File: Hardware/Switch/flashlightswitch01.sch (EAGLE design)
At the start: 11 parts

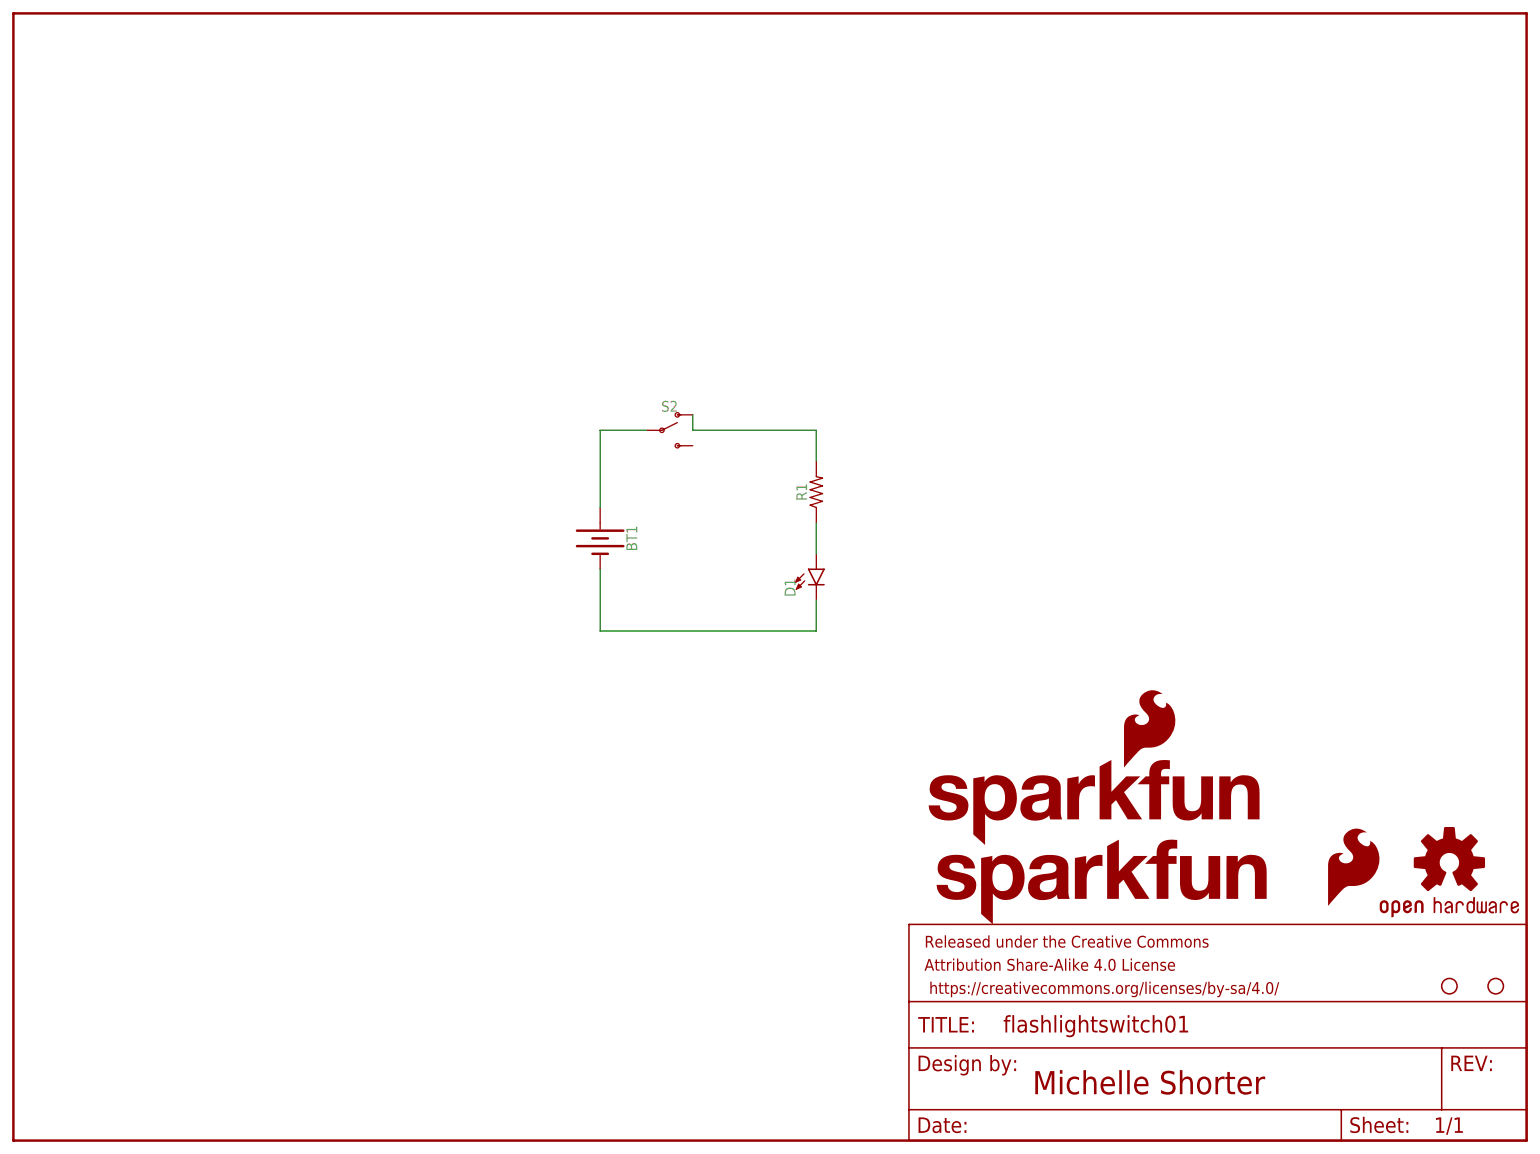
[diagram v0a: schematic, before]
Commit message: Post Proto Review
Added Buzzard labels, changed to different coin cell battery holder, moved schematic to back of board and other changes.
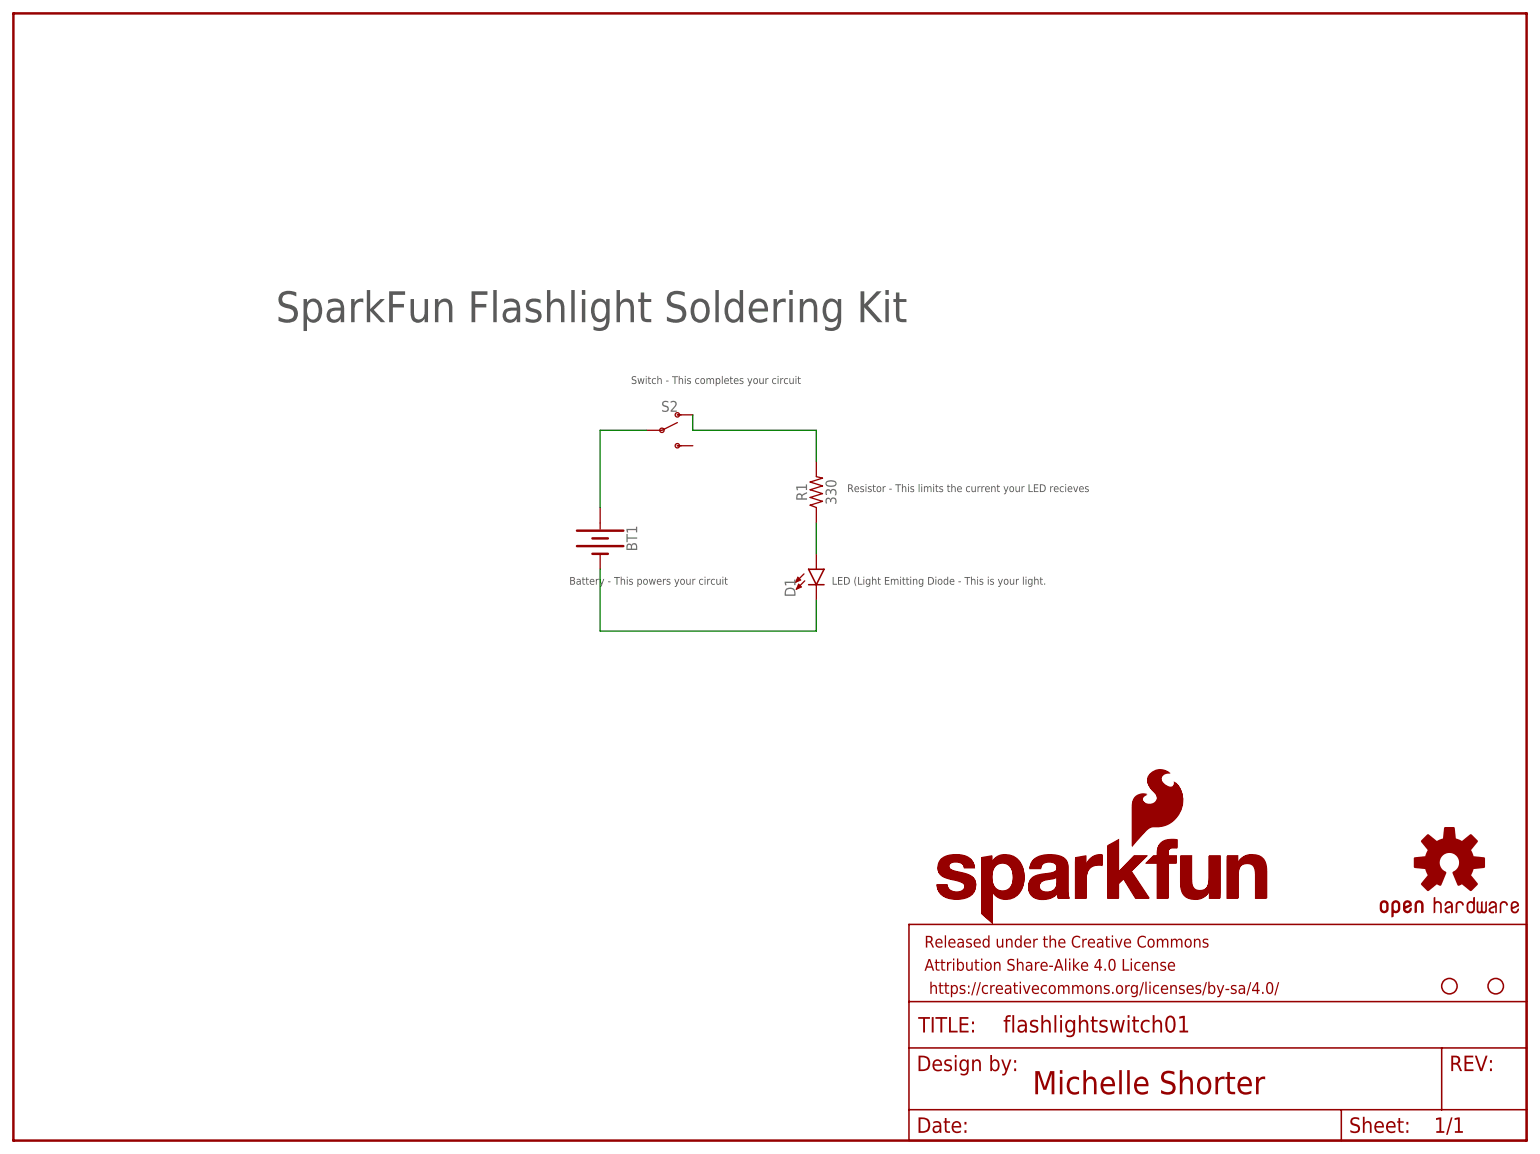
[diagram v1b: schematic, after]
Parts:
- R1: value (none) -> 330
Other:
- note added: "Battery - This powers your circuit"
- note added: "LED (Light Emitting Diode - This is your light."
- note added: "Resistor - This limits the current your LED recieves"
- note added: "SparkFun Flashlight Soldering Kit"
- note added: "Switch - This completes your circuit"
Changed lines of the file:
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@@
 <part name="LOGO1" library="SparkFun-Aesthetics" deviceset="OSHW-LOGO" device="S"/>
 <part name="D1" library="SparkFun-LED" deviceset="LED" device="5MM-KIT"/>
-<part name="R1" library="SparkFun-Resistors" deviceset="RESISTOR" device="AXIAL-0.3-KIT" value=" "/>
+<part name="R1" library="SparkFun-Resistors" deviceset="RESISTOR" device="AXIAL-0.3-KIT" value="330"/>
 <part name="LOGO2" library="SparkFun-Aesthetics" deviceset="SFE_LOGO_FLAME" device=".1_INCH"/>
 <part name="H1" library="SparkFun-Hardware" deviceset="STAND-OFF" device=""/>
@@
 <plain>
 <text x="167.64" y="7.62" size="3.81" layer="94">Michelle Shorter</text>
+<text x="43.18" y="134.62" size="5.08" layer="97" font="vector">SparkFun Flashlight Soldering Kit</text>
+<text x="134.62" y="91.44" size="1.27" layer="97">LED (Light Emitting Diode - This is your light.</text>
+<text x="137.16" y="106.68" size="1.27" layer="97">Resistor - This limits the current your LED recieves</text>
+<text x="101.6" y="124.46" size="1.27" layer="97">Switch - This completes your circuit</text>
+<text x="91.44" y="91.44" size="1.27" layer="97">Battery - This powers your circuit</text>
 </plain>
 <instances>
@@
 <instance part="D1" gate="G$1" x="132.08" y="93.98"/>
 <instance part="R1" gate="G$1" x="132.08" y="106.68" rot="R90"/>
-<instance part="LOGO2" gate="G$1" x="215.9" y="38.1"/>
+<instance part="LOGO2" gate="G$1" x="183.642" y="47.752"/>
 <instance part="H1" gate="G$1" x="236.22" y="25.4"/>
 <instance part="H2" gate="G$1" x="243.84" y="25.4"/>
 <instance part="S2" gate="1" x="106.68" y="116.84"/>
 <instance part="LOGO4" gate="G$1" x="149.86" y="35.56"/>
-<instance part="LOGO3" gate="G$1" x="149.86" y="48.26"/>
+<instance part="LOGO3" gate="G$1" x="151.13" y="35.306"/>
 </instances>
 <busses>
